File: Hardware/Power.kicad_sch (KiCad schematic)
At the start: 20 parts, among them J1 BAT, J2 MOTORES, U1 TPS563252DRLR

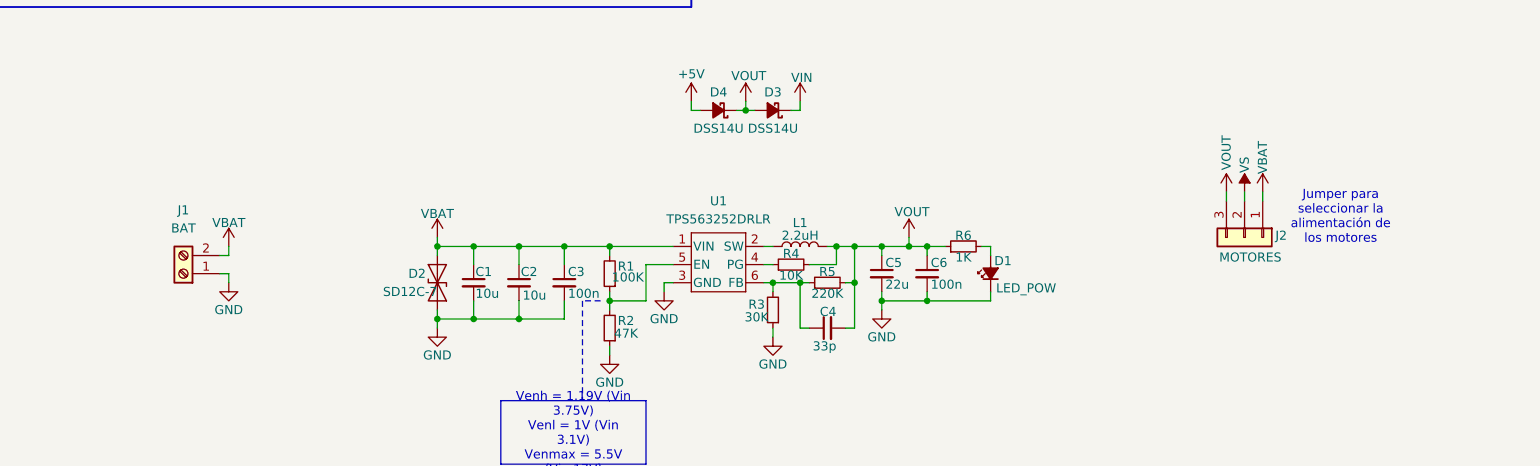
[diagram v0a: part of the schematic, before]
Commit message: Cambio borneras por SMD y elimino jumper de seleción de VS
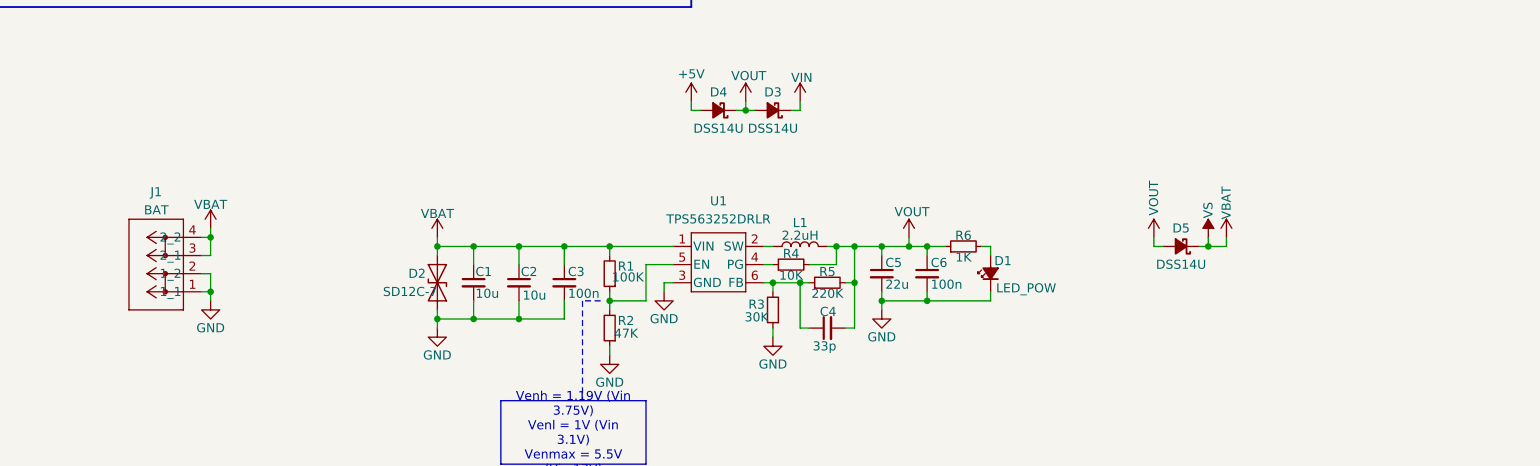
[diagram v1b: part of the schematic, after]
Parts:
- removed J2: MOTORES, Connector_PinHeader_2.54mm:PinHeader_1x03_P2.54mm_Vertical, symbol Connector_Generic:Conn_01x03
- added D5: DSS14U, Diode_SMD:D_SOD-123F, symbol Device:D_Schottky_Small_Filled
- J1: footprint TerminalBlock_RND:TerminalBlock_RND_205-00287_1x02_P5.08mm_Horizontal -> footprints:CONN2_2060-452&slash_998-404_WAG; symbol Connector:Screw_Terminal_01x02 -> 2024-09-06_13-56-18:2060-452_998-404; PartNumber (none) -> 2060-452/998-404; PurchaseLink (none) -> https://www.digikey.com/en/products/detail/wago-corporation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
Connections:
- net GND: now also J1.2 (1_2)
- net VBAT: now also J1.3 (2_1), J1.4 (2_2), D5.1 (K); no longer J1.2 (Pin_2)
- net VOUT: now also D5.2 (A)
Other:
- note removed: "Jumper para seleccionar la alimentación de los motores"

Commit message: Correcciones en el ruteo, agrego fiduciales, 3D y serigrafía
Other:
- company: (none) -> Newsan
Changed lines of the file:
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@@
 	(title_block
 		(title "Archi Bot")
-		(date "2024-07-18")
-		(rev "1.1")
+		(date "2024-09-27")
+		(rev "1.2")
+		(company "Newsan")
 	)
 	(junction

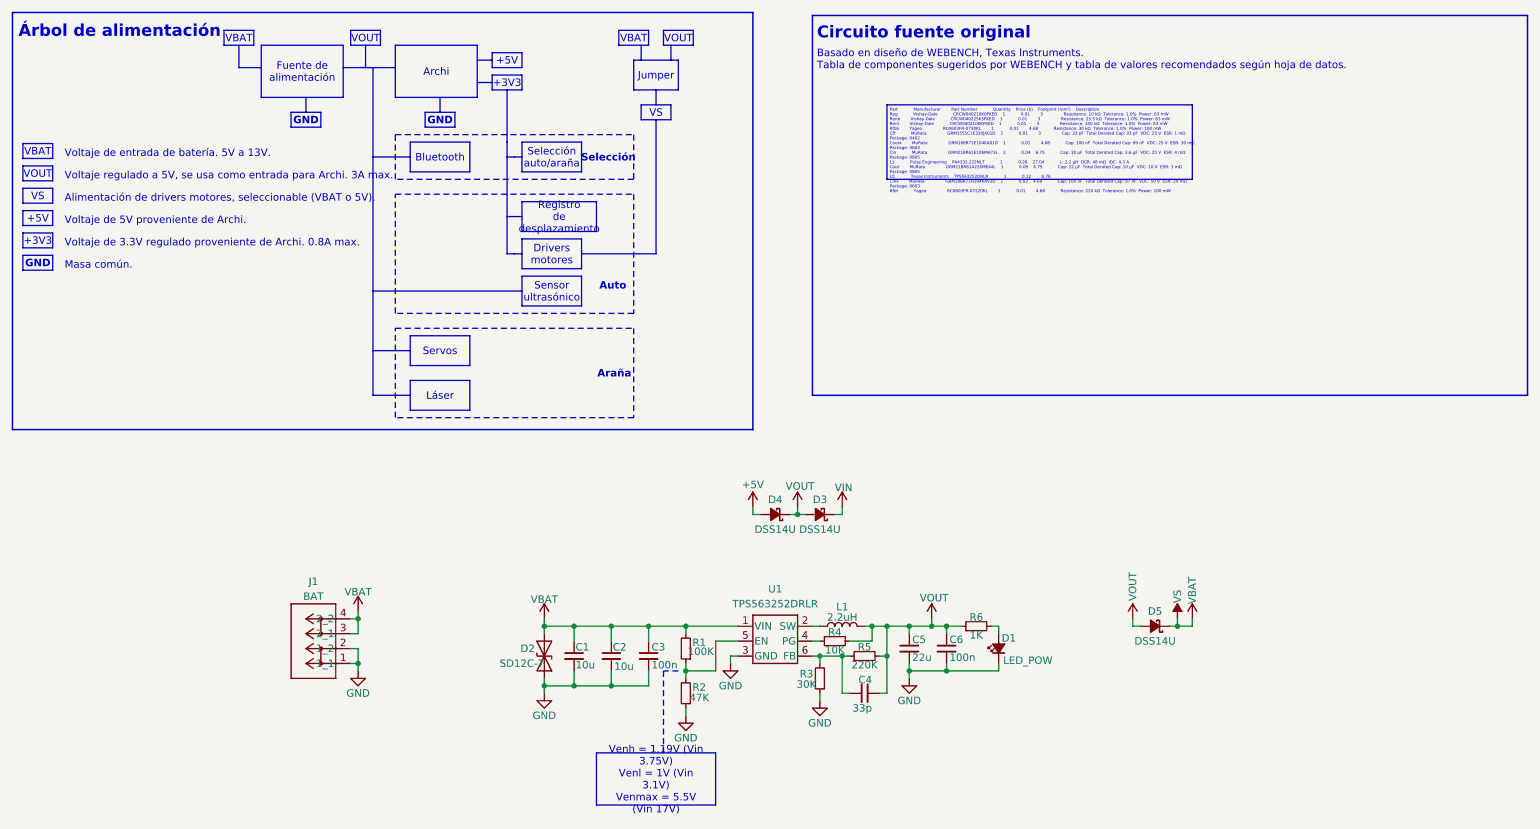
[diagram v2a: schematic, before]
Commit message: Agrego test points, cambio conectores, finalizo v1.2
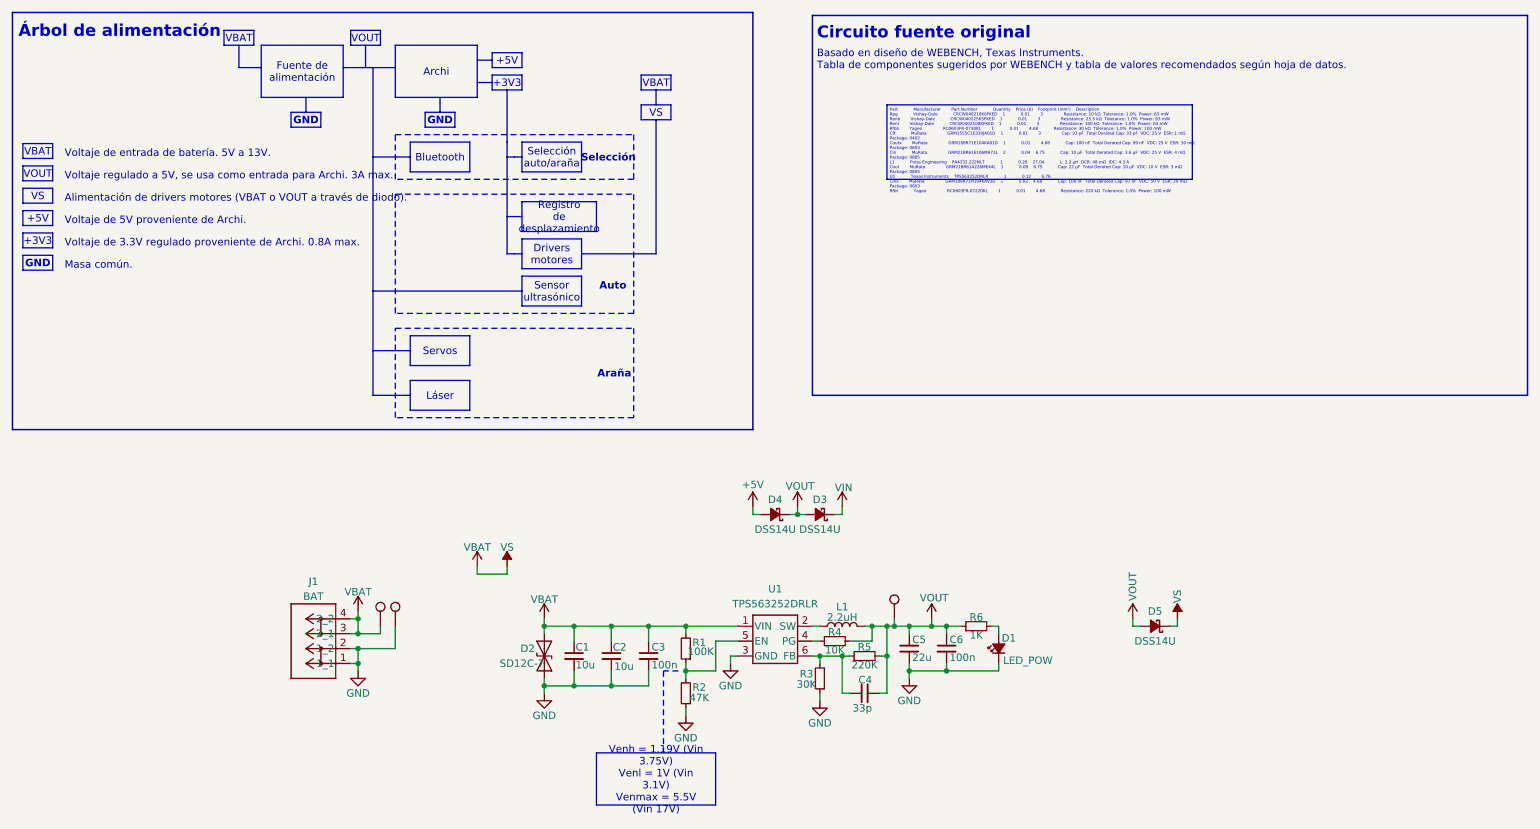
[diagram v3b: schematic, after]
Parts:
- added TP1, TP2, TP3: TestPoint, TestPoint:TestPoint_Pad_D1.0mm, symbol Connector:TestPoint
- J1: footprint footprints:CONN2_2060-452&slash_998-404_WAG -> footprints:CONN2_2060-1452&slash_998-404_WAG
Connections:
- net GND: now also TP2.1
- net VBAT: now also TP1.1
- net VOUT: now also TP3.1
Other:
- note added: "Alimentación de drivers motores (VBAT o VOUT a través de diodo)."
- note removed: "Alimentación de drivers motores, seleccionable (VBAT o 5V)."

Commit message: Agrego archivo faltante al commit anterior
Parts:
- added TP37, TP38: TestPoint, TestPoint:TestPoint_Pad_D1.0mm, symbol Connector:TestPoint
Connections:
- net +5V: now also TP37.1
- net VIN: now also TP38.1
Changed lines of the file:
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@@
 	)
 	(junction
+		(at 142.24 118.11)
+		(diameter 0)
+		(color 0 0 0 0)
+	)
+	(junction
+		(at 157.48 118.11)
+		(diameter 0)
+		(color 0 0 0 0)
+	)
+	(junction
 		(at 165.1 142.24)
 		(diameter 0)
@@
 	(wire
 		(pts
+			(xy 140.97 118.11) (xy 142.24 118.11)
+		)
+		(stroke
+			(width 0)
+			(type default)
+		)
+	)
+	(wire
+		(pts
 			(xy 149.86 118.11) (xy 149.86 116.84)
 		)
@@
 	(wire
 		(pts
+			(xy 157.48 118.11) (xy 158.75 118.11)
+		)
+		(stroke
+			(width 0)
+			(type default)
+		)
+	)
+	(wire
+		(pts
 			(xy 168.91 144.78) (xy 168.91 146.05)
 		)
@@
 	)
 	(symbol
+		(lib_id "Connector:TestPoint")
+		(at 140.97 118.11 90)
+		(unit 1)
+		(exclude_from_sim no)
+		(in_bom yes)
+		(on_board yes)
+		(dnp no)
+		(fields_autoplaced yes)
+		(property "Reference" "TP37"
+			(at 136.3979 115.57 0)
+			(effects
+				(font
+					(size 1.27 1.27)
+				)
+				(justify left)
+				(hide yes)
+			)
+		)
+		(property "Value" "TestPoint"
+			(at 138.9379 115.57 0)
+			(effects
+				(font
+					(size 1.27 1.27)
+				)
+				(justify left)
+				(hide yes)
+			)
+		)
+		(property "Footprint" "TestPoint:TestPoint_Pad_D1.0mm"
+			(at 140.97 113.03 0)
+			(effects
+				(font
+					(size 1.27 1.27)
+				)
+				(hide yes)
+			)
+		)
+		(property "Datasheet" "~"
+			(at 140.97 113.03 0)
+			(effects
+				(font
+					(size 1.27 1.27)
+				)
+				(hide yes)
+			)
+		)
+		(property "Description" "test point"
+			(at 140.97 118.11 0)
+			(effects
+				(font
+					(size 1.27 1.27)
+				)
+				(hide yes)
+			)
+		)
+		(pin "1"
+		)
+		(instances
+			(project "ArchiBot"
+				(path "/e63e39d7-6ac0-4ffd-8aa3-1841a4541b55/5cfd787d-4139-413d-942e-6c87b4316b27"
+					(reference "TP37")
+					(unit 1)
+				)
+			)
+		)
+	)
+	(symbol
 		(lib_id "power:GND")
 		(at 168.91 146.05 0)
@@
 					(unit 1)
 				)
+			)
+		)
+	)
+	(symbol
+		(lib_id "Connector:TestPoint")
+		(at 158.75 118.11 270)
+		(unit 1)
+		(exclude_from_sim no)
+		(in_bom yes)
+		(on_board yes)
+		(dnp no)
+		(fields_autoplaced yes)
+		(property "Reference" "TP38"
+			(at 163.3221 120.65 0)
+			(effects
+				(font
+					(size 1.27 1.27)
+				)
+				(justify left)
+				(hide yes)
+			)
+		)
+		(property "Value" "TestPoint"
+			(at 160.7821 120.65 0)
+			(effects
+				(font
+					(size 1.27 1.27)
+				)
+				(justify left)
+				(hide yes)
+			)
+		)
+		(property "Footprint" "TestPoint:TestPoint_Pad_D1.0mm"
+			(at 158.75 123.19 0)
+			(effects
+				(font
+					(size 1.27 1.27)
+				)
+				(hide yes)
+			)
+		)
+		(property "Datasheet" "~"
+			(at 158.75 123.19 0)
+			(effects
+				(font
+					(size 1.27 1.27)
+				)
+				(hide yes)
+			)
+		)
+		(property "Description" "test point"
+			(at 158.75 118.11 0)
+			(effects
+				(font
+					(size 1.27 1.27)
+				)
+				(hide yes)
+			)
+		)
+		(pin "1"
+		)
+		(instances
+			(project "ArchiBot"
+				(path "/e63e39d7-6ac0-4ffd-8aa3-1841a4541b55/5cfd787d-4139-413d-942e-6c87b4316b27"
+					(reference "TP38")
+					(unit 1)
+				)

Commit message: Actualizo campo descripción
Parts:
- J1: PartNumber 2060-452/998-404 -> 2060-1452/998-404
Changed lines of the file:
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@@
 			)
 		)
-		(property "Description" "Resistor, small symbol"
+		(property "Description" "RES 1K OHM 1% 1/10W 0603"
 			(at 180.34 137.16 0)
 			(effects
@@
 			)
 		)
-		(property "Description" "Resistor, small symbol"
+		(property "Description" "RES 100K OHM 1% 1/10W 0603"
 			(at 130.81 140.97 0)
 			(effects
@@
 			)
 		)
-		(property "Description" "Resistor, small symbol"
+		(property "Description" "RES 10K OHM 1% 1/10W 0603"
 			(at 156.21 139.7 0)
 			(effects
@@
 			)
 		)
-		(property "Description" "Schottky diode, small symbol, filled shape"
+		(property "Description" "DIODE SCHOTTKY 40V 1A SOD123FL"
 			(at 146.05 118.11 0)
 			(effects
@@
 			)
 		)
-		(property "Description" "Resistor, small symbol"
+		(property "Description" "RES 30K OHM 1% 1/10W 0603"
 			(at 153.67 146.05 0)
 			(effects
@@
 			)
 		)
-		(property "Description" "Resistor, small symbol"
+		(property "Description" "RES 220K OHM 1% 1/10W 0603"
 			(at 161.29 142.24 0)
 			(effects
@@
 			)
 		)
-		(property "Description" "Generic screw terminal, single row, 01x02, script generated (kicad-library-utils/schlib/autogen/connector/)"
+		(property "Description" "THR PCB TERMINAL BLOCK; PUSH-BUT 4MM"
 			(at 76.2 143.51 0)
 			(effects
@@
 			)
 		)
-		(property "PartNumber" "2060-452/998-404"
+		(property "PartNumber" "2060-1452/998-404"
 			(at 73.66 143.51 0)
 			(effects
@@
 			)
 		)
-		(property "Description" "Schottky diode, small symbol, filled shape"
+		(property "Description" "DIODE SCHOTTKY 40V 1A SOD123FL"
 			(at 210.82 137.16 0)
 			(effects
@@
 			)
 		)
-		(property "Description" ""
+		(property "Description" "IC REG BUCK ADJ 3A SOT563"
 			(at 134.62 137.16 0)
 			(effects
@@
 			)
 		)
-		(property "Description" "Schottky diode, small symbol, filled shape"
+		(property "Description" "DIODE SCHOTTKY 40V 1A SOD123FL"
 			(at 153.67 118.11 0)
 			(effects
@@
 			)
 		)
-		(property "Description" "Unpolarized capacitor, small symbol"
+		(property "Description" "CAP CER 0.1UF 50V X7R 0603"
 			(at 175.26 140.97 0)
 			(effects
@@
 			)
 		)
-		(property "Description" "Unpolarized capacitor, small symbol"
+		(property "Description" "CAP CER 10UF 25V X5R 0805"
 			(at 118.11 142.24 0)
 			(effects
@@
 			)
 		)
-		(property "Description" "Unpolarized capacitor, small symbol"
+		(property "Description" "CAP CER 22UF 25V X5R 0805"
 			(at 168.91 140.97 0)
 			(effects
@@
 			)
 		)
-		(property "Description" "Light emitting diode, small symbol, filled shape"
+		(property "Description" "LED GREEN DIFFUSED 0603 SMD"
 			(at 184.15 140.97 0)
 			(effects
@@
 			)
 		)
-		(property "Description" "Unpolarized capacitor, small symbol"
+		(property "Description" "CAP CER 10UF 25V X5R 0805"
 			(at 111.76 142.24 0)
 			(effects
@@
 			)
 		)
-		(property "Description" "Unpolarized capacitor, small symbol"
+		(property "Description" "CAP CER 0.1UF 50V X7R 0603"
 			(at 124.46 142.24 0)
 			(effects
@@
 			)
 		)
-		(property "Description" "Inductor"
+		(property "Description" "FIXED IND 2.2UH 4.3A 48 MOHM SMD"
 			(at 157.48 137.16 0)
 			(effects
@@
 			)
 		)
-		(property "Description" "Unpolarized capacitor, small symbol"
+		(property "Description" "CAP CER 33PF 50V C0G/NP0 0402"
 			(at 161.29 148.59 0)
 			(effects
@@
 			)
 		)
-		(property "Description" "Resistor, small symbol"
+		(property "Description" "RES 47K OHM 1% 1/10W 0603"
 			(at 130.81 148.59 0)
 			(effects
@@
 			)
 		)
-		(property "Description" "12V, 450W Discrete Bidirectional TVS Diode, SOD-323"
+		(property "Description" "TVS DIODE 12VWM 24VC SOD323"
 			(at 106.68 142.24 0)
 			(effects

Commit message: Agrego campos manufacturer y package
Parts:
- C1, C2: Manufacturer (none) -> Murata Electronics; Package (none) -> 0805 (2012 Metric)
- C3, C6: Manufacturer (none) -> Samsung Electro-Mechanics; Package (none) -> 0603 (1608 Metric)
- C4: Manufacturer (none) -> Murata Electronics; Package (none) -> 0402 (1005 Metric)
- C5: Manufacturer (none) -> Samsung Electro-Mechanics; Package (none) -> 0805 (2012 Metric)
- D1: Manufacturer (none) -> Harvatek Corporation; Package (none) -> 0603 (1608 Metric)
- D2: Manufacturer (none) -> Diodes Incorporated; Package (none) -> SC-76, SOD-323
- D3, D4, D5: Manufacturer (none) -> SMC Diode Solutions; Package (none) -> SOD-123FL
- J1: Manufacturer (none) -> WAGO Corporation; Package (none) -> 0.157" (4.00mm)
- L1: Manufacturer (none) -> Pulse Electronics; Package (none) -> Nonstandard (4.20mm x 4.20mm)
- R1, R2, R3, R4, R5, R6: Manufacturer (none) -> YAGEO; Package (none) -> 0603 (1608 Metric)
- U1: Manufacturer (none) -> Texas Instruments; Package (none) -> SOT-563, SOT-666
